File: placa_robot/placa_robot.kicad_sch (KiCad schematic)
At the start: 39 parts, among them IC1 MSP430FR2355TPT, J1 Conn_01x03, J2 Conn_01x04, J3 Conn_02x04_Odd_Even, J4 conn_DFrobot, SW1 SW_Push, U3 LMV324, U4 LMV324, Y1 Crystal

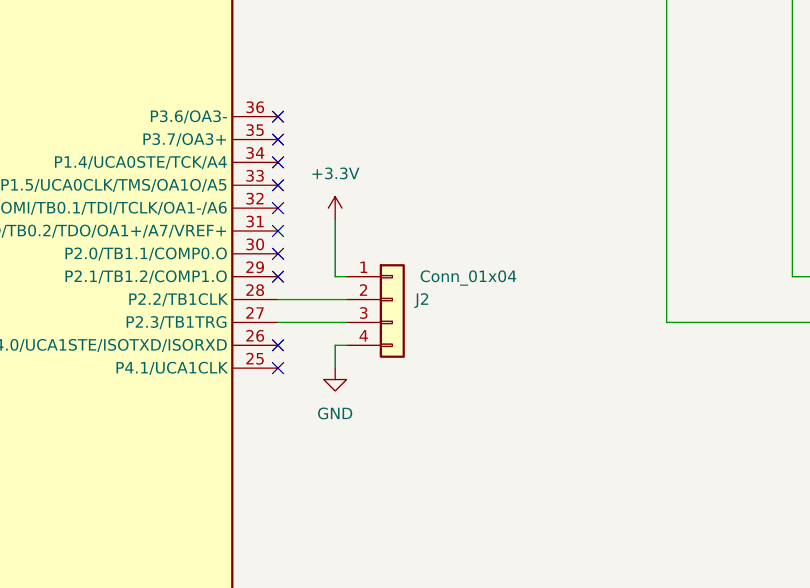
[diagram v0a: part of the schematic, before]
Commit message: Borrar connector
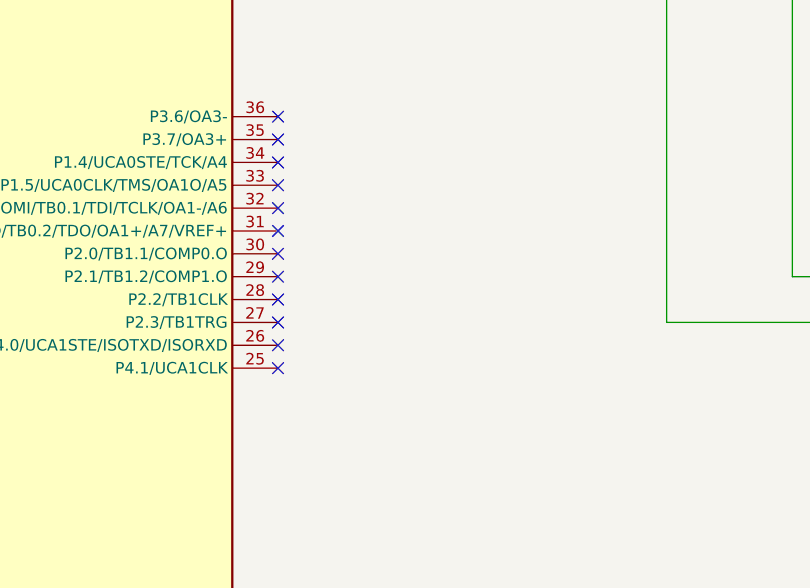
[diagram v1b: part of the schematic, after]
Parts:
- removed J2: Conn_01x04, symbol Connector_Generic:Conn_01x04
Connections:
- no-connect marks 39 -> 41

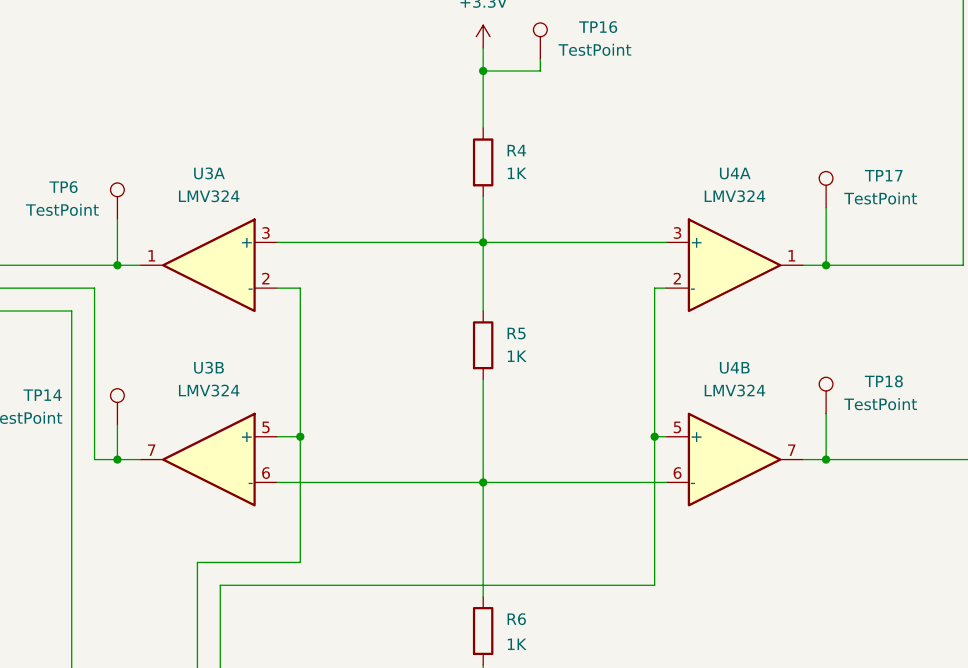
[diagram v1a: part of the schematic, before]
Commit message: Huellas menos LCD, SW y jumper
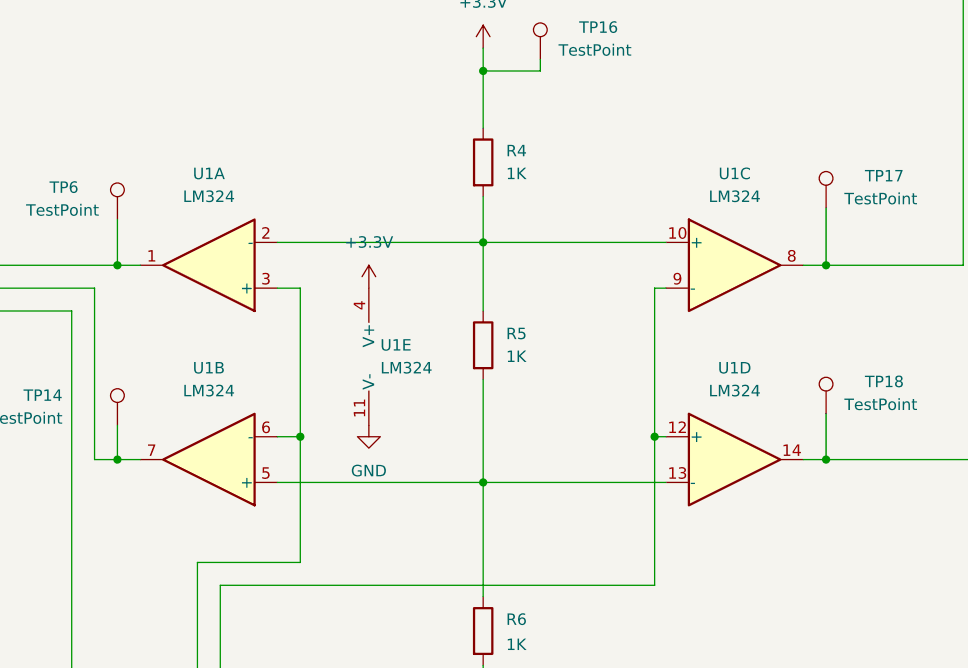
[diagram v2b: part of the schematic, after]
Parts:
- removed U3, U4: LMV324, symbol Amplifier_Operational:LMV324
- added U1: LM324, Package_SO:SOIC-14_3.9x8.7mm_P1.27mm, symbol Amplifier_Operational:LM324
- C2, C3, C4, C5: footprint (none) -> Capacitor_SMD:C_0805_2012Metric_Pad1.18x1.45mm_HandSolder
- J1: footprint (none) -> Connector_PinHeader_2.54mm:PinHeader_1x03_P2.54mm_Vertical
- J3: footprint (none) -> Connector_PinHeader_2.54mm:PinHeader_2x04_P2.54mm_Vertical
- R10, R13, R14, R15, R16, R4, R5, R6, R9: footprint (none) -> Resistor_SMD:R_0805_2012Metric_Pad1.20x1.40mm_HandSolder
- TP1, TP10, TP11, TP12, TP13, TP14, TP15, TP16, TP17, TP18, TP2, TP6: footprint (none) -> Connector_PinHeader_2.54mm:PinHeader_1x01_P2.54mm_Vertical
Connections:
- net +3.3V: now also U1.4 (V+)
- net GND: now also U1.11 (V-)
- net at S2.2: now also U1.12 (+), U1.9 (-)
- net at R5.2, R6.1: now also U1.13 (-), U1.5 (+)
- net at IC1.46 (P3.1/OA2O), TP18.1: now also U1.14
- net at R4.2, R5.1: now also U1.10 (+), U1.2 (-)
- net at IC1.44 (P3.3/OA2+), TP6.1: now also U1.1
- net at IC1.38 (P3.4/SMCLK), TP14.1: now also U1.7
- net at IC1.45 (P3.2/OA2-), TP17.1: now also U1.8
- net at S2.12 (2'): now also U1.3 (+), U1.6 (-)
